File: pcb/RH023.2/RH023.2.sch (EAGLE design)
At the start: 31 parts, among them CN1 USB, U2 FT232RLSSOP, U3 REG1117

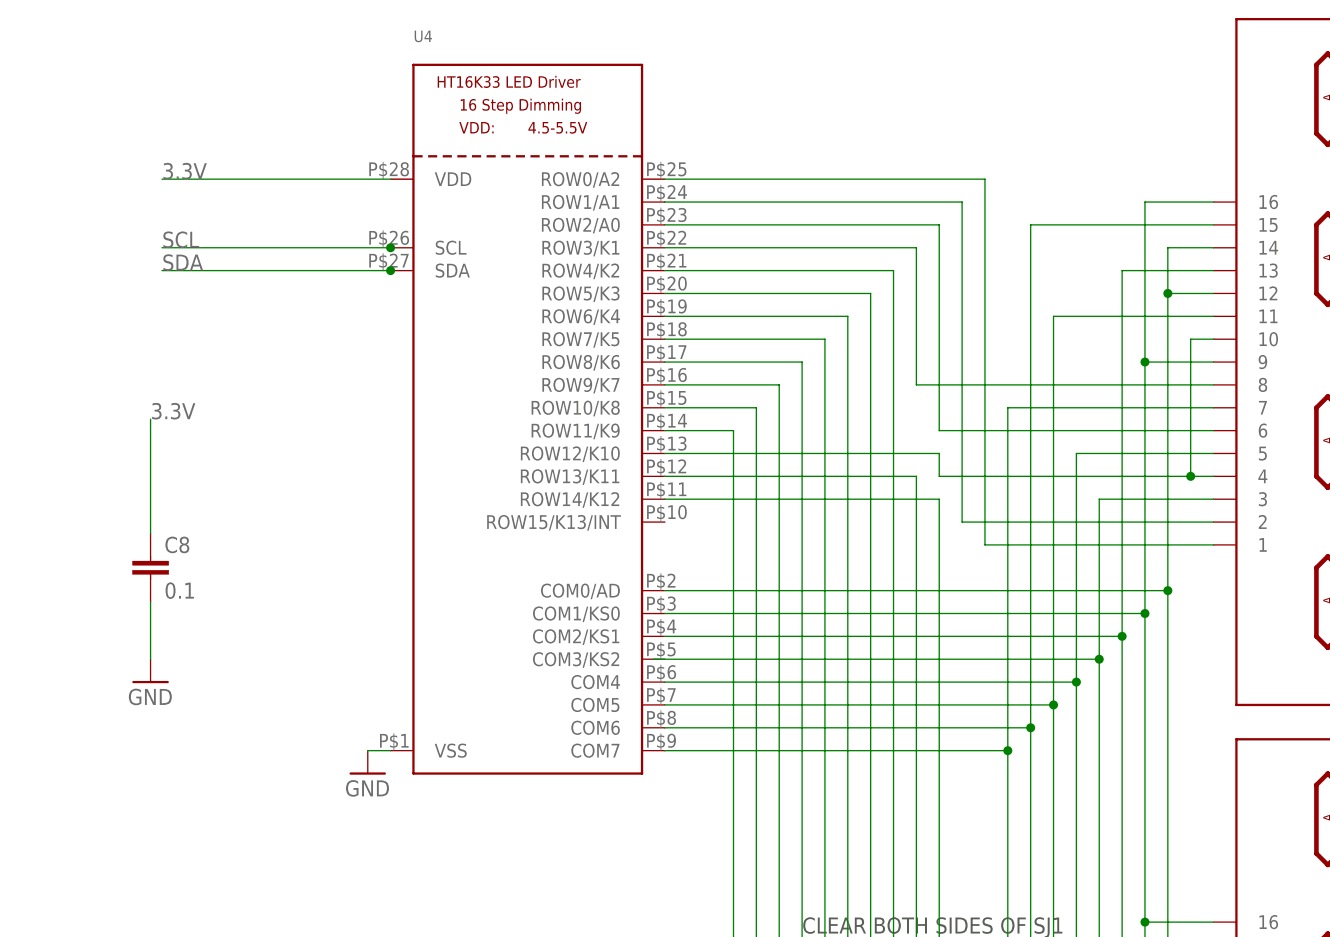
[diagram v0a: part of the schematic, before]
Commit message: fixed unattached nets
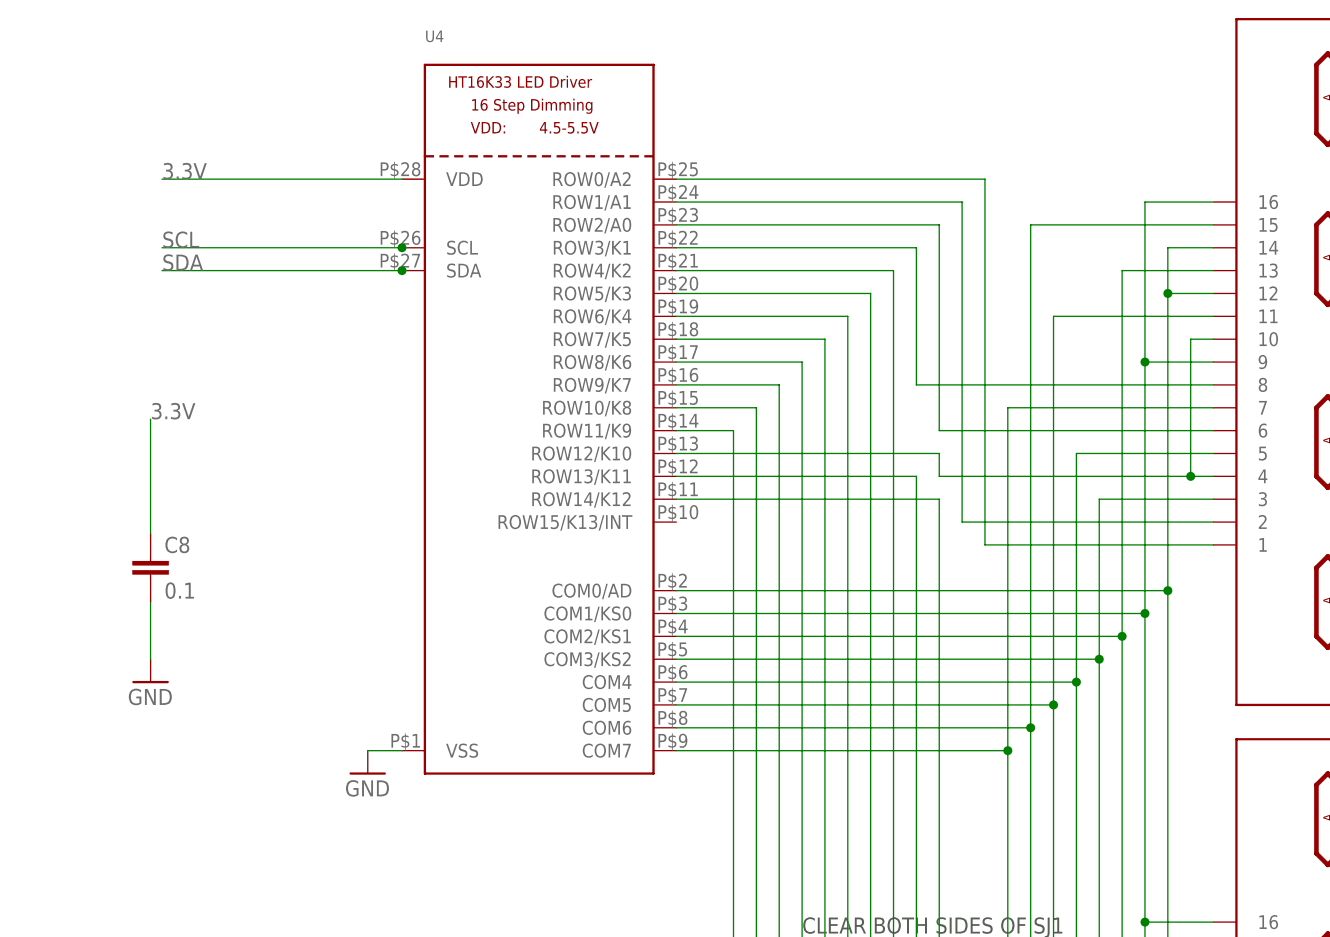
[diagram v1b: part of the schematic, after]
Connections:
- net N$19: now also LED5.1
- net N$6: now also U4.COM3/KS2
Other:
- moved on the sheet: U4
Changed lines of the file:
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@@
 <instance part="SJ23" gate="1" x="125.73" y="58.42"/>
 <instance part="SJ24" gate="1" x="125.73" y="45.72"/>
-<instance part="U4" gate="G$1" x="317.5" y="134.62"/>
+<instance part="U4" gate="G$1" x="318.77" y="134.62"/>
 <instance part="GND1" gate="1" x="299.72" y="93.98"/>
 <instance part="GND2" gate="1" x="275.59" y="104.14"/>
@@
 </segment>
 <segment>
-<wire x1="299.72" y1="96.52" x2="302.26" y2="96.52" width="0.1524" layer="91"/>
 <pinref part="U4" gate="G$1" pin="VSS"/>
 <pinref part="GND1" gate="1" pin="GND"/>
+<wire x1="303.53" y1="96.52" x2="299.72" y2="96.52" width="0.1524" layer="91"/>
 </segment>
 <segment>
@@
 <segment>
 <pinref part="U4" gate="G$1" pin="VDD"/>
-<wire x1="302.26" y1="160.02" x2="276.86" y2="160.02" width="0.1524" layer="91"/>
+<wire x1="303.53" y1="160.02" x2="276.86" y2="160.02" width="0.1524" layer="91"/>
 <label x="276.86" y="160.02" size="1.778" layer="95"/>
 </segment>
@@
 </segment>
 <segment>
-<wire x1="302.26" y1="152.4" x2="276.86" y2="152.4" width="0.1524" layer="91"/>
-<junction x="302.26" y="152.4"/>
+<wire x1="303.53" y1="152.4" x2="276.86" y2="152.4" width="0.1524" layer="91"/>
+<junction x="303.53" y="152.4"/>
 <pinref part="U4" gate="G$1" pin="SCL"/>
 <label x="276.86" y="152.4" size="1.778" layer="95"/>
@@
 </segment>
 <segment>
-<wire x1="302.26" y1="149.86" x2="276.86" y2="149.86" width="0.1524" layer="91"/>
-<junction x="302.26" y="149.86"/>
+<wire x1="303.53" y1="149.86" x2="276.86" y2="149.86" width="0.1524" layer="91"/>
+<junction x="303.53" y="149.86"/>
 <pinref part="U4" gate="G$1" pin="SDA"/>
 <label x="276.86" y="149.86" size="1.778" layer="95"/>
@@
 <segment>
 <pinref part="U4" gate="G$1" pin="COM0/AD"/>
-<wire x1="332.74" y1="114.3" x2="388.62" y2="114.3" width="0.1524" layer="91"/>
+<wire x1="334.01" y1="114.3" x2="388.62" y2="114.3" width="0.1524" layer="91"/>
 <wire x1="388.62" y1="114.3" x2="388.62" y2="147.32" width="0.1524" layer="91"/>
 <pinref part="LED3" gate="G$1" pin="14"/>
@@
 <segment>
 <pinref part="U4" gate="G$1" pin="COM1/KS0"/>
-<wire x1="332.74" y1="111.76" x2="386.08" y2="111.76" width="0.1524" layer="91"/>
+<wire x1="334.01" y1="111.76" x2="386.08" y2="111.76" width="0.1524" layer="91"/>
 <wire x1="386.08" y1="111.76" x2="386.08" y2="139.7" width="0.1524" layer="91"/>
 <pinref part="LED3" gate="G$1" pin="16"/>
@@
 <segment>
 <pinref part="U4" gate="G$1" pin="COM2/KS1"/>
-<wire x1="332.74" y1="109.22" x2="383.54" y2="109.22" width="0.1524" layer="91"/>
+<wire x1="334.01" y1="109.22" x2="383.54" y2="109.22" width="0.1524" layer="91"/>
 <wire x1="383.54" y1="109.22" x2="383.54" y2="149.86" width="0.1524" layer="91"/>
 <pinref part="LED3" gate="G$1" pin="13"/>
@@
 <net name="N$6" class="0">
 <segment>
-<wire x1="331.47" y1="106.68" x2="381" y2="106.68" width="0.1524" layer="91"/>
+<wire x1="334.01" y1="106.68" x2="381" y2="106.68" width="0.1524" layer="91"/>
 <wire x1="381" y1="106.68" x2="381" y2="124.46" width="0.1524" layer="91"/>
 <pinref part="LED3" gate="G$1" pin="3"/>
@@
 <wire x1="381" y1="-34.29" x2="381" y2="44.45" width="0.1524" layer="91"/>
 <junction x="381" y="44.45"/>
+<pinref part="U4" gate="G$1" pin="COM3/KS2"/>
 </segment>
 </net>
@@
 <segment>
 <pinref part="U4" gate="G$1" pin="COM4"/>
-<wire x1="332.74" y1="104.14" x2="378.46" y2="104.14" width="0.1524" layer="91"/>
+<wire x1="334.01" y1="104.14" x2="378.46" y2="104.14" width="0.1524" layer="91"/>
 <wire x1="378.46" y1="104.14" x2="378.46" y2="129.54" width="0.1524" layer="91"/>
 <pinref part="LED3" gate="G$1" pin="5"/>
@@
 <segment>
 <pinref part="U4" gate="G$1" pin="COM5"/>
-<wire x1="332.74" y1="101.6" x2="375.92" y2="101.6" width="0.1524" layer="91"/>
+<wire x1="334.01" y1="101.6" x2="375.92" y2="101.6" width="0.1524" layer="91"/>
 <wire x1="375.92" y1="101.6" x2="375.92" y2="144.78" width="0.1524" layer="91"/>
 <pinref part="LED3" gate="G$1" pin="11"/>
@@
 <segment>
 <pinref part="U4" gate="G$1" pin="COM6"/>
-<wire x1="332.74" y1="99.06" x2="373.38" y2="99.06" width="0.1524" layer="91"/>
+<wire x1="334.01" y1="99.06" x2="373.38" y2="99.06" width="0.1524" layer="91"/>
 <wire x1="373.38" y1="99.06" x2="373.38" y2="154.94" width="0.1524" layer="91"/>
 <pinref part="LED3" gate="G$1" pin="15"/>
@@
 <segment>
 <pinref part="U4" gate="G$1" pin="COM7"/>
-<wire x1="332.74" y1="96.52" x2="370.84" y2="96.52" width="0.1524" layer="91"/>
+<wire x1="334.01" y1="96.52" x2="370.84" y2="96.52" width="0.1524" layer="91"/>
 <wire x1="370.84" y1="96.52" x2="370.84" y2="134.62" width="0.1524" layer="91"/>
 <pinref part="LED3" gate="G$1" pin="7"/>
@@
 <segment>
 <pinref part="U4" gate="G$1" pin="ROW0/A2"/>
-<wire x1="332.74" y1="160.02" x2="368.3" y2="160.02" width="0.1524" layer="91"/>
+<wire x1="334.01" y1="160.02" x2="368.3" y2="160.02" width="0.1524" layer="91"/>
 <wire x1="368.3" y1="160.02" x2="368.3" y2="119.38" width="0.1524" layer="91"/>
 <pinref part="LED3" gate="G$1" pin="1"/>
@@
 <wire x1="365.76" y1="121.92" x2="365.76" y2="157.48" width="0.1524" layer="91"/>
 <pinref part="U4" gate="G$1" pin="ROW1/A1"/>
-<wire x1="365.76" y1="157.48" x2="332.74" y2="157.48" width="0.1524" layer="91"/>
+<wire x1="365.76" y1="157.48" x2="334.01" y2="157.48" width="0.1524" layer="91"/>
 </segment>
 </net>
@@
 <segment>
 <pinref part="U4" gate="G$1" pin="ROW2/A0"/>
-<wire x1="332.74" y1="154.94" x2="363.22" y2="154.94" width="0.1524" layer="91"/>
+<wire x1="334.01" y1="154.94" x2="363.22" y2="154.94" width="0.1524" layer="91"/>
 <wire x1="363.22" y1="154.94" x2="363.22" y2="132.08" width="0.1524" layer="91"/>
 <pinref part="LED3" gate="G$1" pin="6"/>
@@
 <wire x1="360.68" y1="137.16" x2="360.68" y2="152.4" width="0.1524" layer="91"/>
 <pinref part="U4" gate="G$1" pin="ROW3/K1"/>
-<wire x1="360.68" y1="152.4" x2="332.74" y2="152.4" width="0.1524" layer="91"/>
+<wire x1="360.68" y1="152.4" x2="334.01" y2="152.4" width="0.1524" layer="91"/>
 </segment>
 </net>
@@
 <segment>
 <pinref part="U4" gate="G$1" pin="ROW4/K2"/>
-<wire x1="332.74" y1="149.86" x2="358.14" y2="149.86" width="0.1524" layer="91"/>
+<wire x1="334.01" y1="149.86" x2="358.14" y2="149.86" width="0.1524" layer="91"/>
 <wire x1="358.14" y1="149.86" x2="358.14" y2="39.37" width="0.1524" layer="91"/>
 <pinref part="LED4" gate="G$1" pin="1"/>
@@
 <wire x1="355.6" y1="41.91" x2="355.6" y2="147.32" width="0.1524" layer="91"/>
 <pinref part="U4" gate="G$1" pin="ROW5/K3"/>
-<wire x1="355.6" y1="147.32" x2="332.74" y2="147.32" width="0.1524" layer="91"/>
+<wire x1="355.6" y1="147.32" x2="334.01" y2="147.32" width="0.1524" layer="91"/>
 </segment>
 </net>
@@
 <segment>
 <pinref part="U4" gate="G$1" pin="ROW6/K4"/>
-<wire x1="332.74" y1="144.78" x2="353.06" y2="144.78" width="0.1524" layer="91"/>
+<wire x1="334.01" y1="144.78" x2="353.06" y2="144.78" width="0.1524" layer="91"/>
 <wire x1="353.06" y1="144.78" x2="353.06" y2="52.07" width="0.1524" layer="91"/>
 <pinref part="LED4" gate="G$1" pin="6"/>
@@
 <wire x1="350.52" y1="57.15" x2="350.52" y2="142.24" width="0.1524" layer="91"/>
 <pinref part="U4" gate="G$1" pin="ROW7/K5"/>
-<wire x1="350.52" y1="142.24" x2="332.74" y2="142.24" width="0.1524" layer="91"/>
+<wire x1="350.52" y1="142.24" x2="334.01" y2="142.24" width="0.1524" layer="91"/>
 </segment>
 </net>
@@
 <segment>
 <pinref part="U4" gate="G$1" pin="ROW8/K6"/>
-<wire x1="332.74" y1="139.7" x2="347.98" y2="139.7" width="0.1524" layer="91"/>
+<wire x1="334.01" y1="139.7" x2="347.98" y2="139.7" width="0.1524" layer="91"/>
 <wire x1="347.98" y1="139.7" x2="347.98" y2="-39.37" width="0.1524" layer="91"/>
 <wire x1="347.98" y1="-39.37" x2="393.7" y2="-39.37" width="0.1524" layer="91"/>
+<pinref part="LED5" gate="G$1" pin="1"/>
 </segment>
 </net>
@@
 <wire x1="345.44" y1="-36.83" x2="345.44" y2="137.16" width="0.1524" layer="91"/>
 <pinref part="U4" gate="G$1" pin="ROW9/K7"/>
-<wire x1="345.44" y1="137.16" x2="332.74" y2="137.16" width="0.1524" layer="91"/>
+<wire x1="345.44" y1="137.16" x2="334.01" y2="137.16" width="0.1524" layer="91"/>
 </segment>
 </net>
@@
 <segment>
 <pinref part="U4" gate="G$1" pin="ROW10/K8"/>
-<wire x1="332.74" y1="134.62" x2="342.9" y2="134.62" width="0.1524" layer="91"/>
+<wire x1="334.01" y1="134.62" x2="342.9" y2="134.62" width="0.1524" layer="91"/>
 <wire x1="342.9" y1="134.62" x2="342.9" y2="-26.67" width="0.1524" layer="91"/>
 <pinref part="LED5" gate="G$1" pin="6"/>
@@
 <wire x1="340.36" y1="-21.59" x2="340.36" y2="132.08" width="0.1524" layer="91"/>
 <pinref part="U4" gate="G$1" pin="ROW11/K9"/>
-<wire x1="340.36" y1="132.08" x2="332.74" y2="132.08" width="0.1524" layer="91"/>
+<wire x1="340.36" y1="132.08" x2="334.01" y2="132.08" width="0.1524" layer="91"/>
 </segment>
 </net>
@@
 <segment>
 <pinref part="U4" gate="G$1" pin="ROW12/K10"/>
-<wire x1="332.74" y1="129.54" x2="363.22" y2="129.54" width="0.1524" layer="91"/>
+<wire x1="334.01" y1="129.54" x2="363.22" y2="129.54" width="0.1524" layer="91"/>
 <wire x1="363.22" y1="129.54" x2="363.22" y2="127" width="0.1524" layer="91"/>
 <pinref part="LED3" gate="G$1" pin="4"/>
@@
 <wire x1="391.16" y1="46.99" x2="393.7" y2="46.99" width="0.1524" layer="91"/>
 <pinref part="U4" gate="G$1" pin="ROW13/K11"/>
-<wire x1="332.74" y1="127" x2="360.68" y2="127" width="0.1524" layer="91"/>
+<wire x1="334.01" y1="127" x2="360.68" y2="127" width="0.1524" layer="91"/>
 <wire x1="360.68" y1="127" x2="360.68" y2="62.23" width="0.1524" layer="91"/>
 <wire x1="360.68" y1="62.23" x2="391.16" y2="62.23" width="0.1524" layer="91"/>
@@
 <wire x1="391.16" y1="-31.75" x2="393.7" y2="-31.75" width="0.1524" layer="91"/>
 <pinref part="U4" gate="G$1" pin="ROW14/K12"/>
-<wire x1="332.74" y1="124.46" x2="363.22" y2="124.46" width="0.1524" layer="91"/>
+<wire x1="334.01" y1="124.46" x2="363.22" y2="124.46" width="0.1524" layer="91"/>
 <wire x1="363.22" y1="124.46" x2="363.22" y2="-16.51" width="0.1524" layer="91"/>
 <wire x1="363.22" y1="-16.51" x2="391.16" y2="-16.51" width="0.1524" layer="91"/>
